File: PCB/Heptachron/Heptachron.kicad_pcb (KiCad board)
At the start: 2 copper layers, 50 x 42 mm, 13 parts, among them J1 Conn_01x06_Pin, J2 Conn_01x06_Pin

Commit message: Test PCB finished!
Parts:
- removed J2: Conn_01x06_Pin, Connector_Wire:SolderWire-0.1sqmm_1x06_P3.6mm_D0.4mm_OD1mm_Relief
- added C1: 100n, Capacitor_SMD:C_0603_1608Metric, F.Cu at (168.6, 119.5)
- added C2: 4.7u, Capacitor_SMD:C_0805_2012Metric, F.Cu at (125.5, 84.8)
- added C3: 4.7u, Capacitor_SMD:C_0805_2012Metric, F.Cu at (135.7, 81.5)
- added C4: 100n, Capacitor_SMD:C_0603_1608Metric, F.Cu at (147.5, 115.5)
- added C5: 4.7u, Capacitor_SMD:C_0805_2012Metric, F.Cu at (130.8, 88.5)
- added C6: 100n, Capacitor_SMD:C_0603_1608Metric, F.Cu at (127.1, 109.3)
- added C7: 100n, Capacitor_SMD:C_0603_1608Metric, F.Cu at (156.8, 90.7)
- added D1: PGD, LED_SMD:LED_0603_1608Metric, F.Cu at (146.1, 79.5)
- added D2: CHG, LED_SMD:LED_0603_1608Metric, F.Cu at (142.2, 79.5)
- added D3: BAT, LED_SMD:LED_0603_1608Metric, F.Cu at (154.0, 79.5)
- added D4: VCC, LED_SMD:LED_0603_1608Metric, F.Cu at (150.1, 79.5)
- added Q1: Q_Photo, LED_SMD:LED_0603_1608Metric, F.Cu at (133.2, 109.2)
- added R1: 10K, Resistor_SMD:R_0603_1608Metric, F.Cu at (165.7, 122.7)
- added R10: 1K, Resistor_SMD:R_0603_1608Metric, F.Cu at (142.2, 77.6)
- added R11: 1K, Resistor_SMD:R_0603_1608Metric, F.Cu at (154.0, 77.6)
- added R12: 1K, Resistor_SMD:R_0603_1608Metric, F.Cu at (150.1, 77.6)
- added R13: 2K, Resistor_SMD:R_0603_1608Metric, F.Cu at (153.9, 126.3)
- added R14: 2K, Resistor_SMD:R_0603_1608Metric, F.Cu at (153.9, 123.1)
- added R15: 10K, Resistor_SMD:R_0603_1608Metric, F.Cu at (159.7, 93.6)
- added R16: 10K, Resistor_SMD:R_0603_1608Metric, F.Cu at (130.1, 109.2)
- added R2: 10K, Resistor_SMD:R_0603_1608Metric, F.Cu at (165.7, 116.5)
- added R3: 10K, Resistor_SMD:R_0603_1608Metric, F.Cu at (125.5, 81.2)
- added R4: 10K, Resistor_SMD:R_0603_1608Metric, F.Cu at (125.5, 82.9)
- added R5: 3.3K, Resistor_SMD:R_0603_1608Metric, F.Cu at (128.8, 88.3)
- added R6: 4.7K, Resistor_SMD:R_0603_1608Metric, F.Cu at (135.7, 85.2)
- added R7: DNP, Resistor_SMD:R_0603_1608Metric, F.Cu at (132.7, 88.4)
- added R8: 10K, Resistor_SMD:R_0603_1608Metric, F.Cu at (135.7, 83.5)
- added R9: 1K, Resistor_SMD:R_0603_1608Metric, F.Cu at (146.1, 77.6)
- added SW1: SW_Push, Button_Switch_SMD:SW_Push_1P1T_NO_6x6mm_H9.5mm, F.Cu at (136.2, 126.5)
- added SW2: SW_Push, Button_Switch_SMD:SW_Push_1P1T_NO_6x6mm_H9.5mm, F.Cu at (125.5, 126.5)
- added SW4: SW_SP3T, Heptachron-Lib:sp3t_jumpers, F.Cu at (121.7, 90.3)
- added U6: BQ24230RGT, Package_DFN_QFN:VQFN-16-1EP_3x3mm_P0.5mm_EP1.68x1.68mm_ThermalVias, F.Cu at (130.8, 83.3)
- added U7: IS31FL3729, Package_QFP:TQFP-32_7x7mm_P0.8mm, F.Cu at (163.5, 86.9)
- added U8: ATtiny424-SS, Package_SO:SOIC-14_3.9x8.7mm_P1.27mm, F.Cu at (147.5, 121.5)
- added X1: RV-3028-C7, Heptachron-Lib:RV-3028-C7, F.Cu at (165.7, 119.5)
- J1: value Conn_01x06_Pin -> Conn_02x03_Counter_Clockwise; footprint Connector_Wire:SolderWire-0.1sqmm_1x06_P3.6mm_D0.4mm_OD1mm_Relief -> Connector_PinHeader_2.54mm:PinHeader_2x03_P2.54mm_Vertical
- moved D38 8.00 mm to (152.0, 108.0), turned to -90 degrees
- moved D42 8.00 mm to (144.0, 108.0), turned to -90 degrees
- moved J1 7.10 mm to (131.3, 120.3), turned to 180 degrees
- moved D39 4.00 mm to (150.0, 108.0), turned to -90 degrees
- moved D41 4.00 mm to (146.0, 108.0), turned to -90 degrees
- turned D40 to -90 degrees
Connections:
- D36 pad 1: /CS5 -> /CS7
- D36 pad 2: /SW6 -> /SW5
- D37 pad 1: /CS5 -> /CS6
- D37 pad 2: /SW7 -> /SW5
- D38 pad 1: /CS5 -> /CS1
- D38 pad 2: /SW1 -> /SW5
- D39 pad 1: /CS5 -> /CS2
- D39 pad 2: /SW2 -> /SW5
- D40 pad 1: /CS5 -> /CS3
- D40 pad 2: /SW3 -> /SW5
- D41 pad 1: /CS5 -> /CS4
- D41 pad 2: /SW4 -> /SW5
- J1 pad 1: /SW1 -> /UPDI
- J1 pad 2: /SW2 -> +BATT
- J1 pad 3: /SW3 -> /TX
- J1 pad 4: /SW4 -> +5V
- J1 pad 5: /SW5 -> /RX
- J1 pad 6: /SW6 -> GND
- U1 pad 1: /SW1 -> /SW4
- U1 pad 10: /CS1 -> /CS3
- U1 pad 11: /CS1 -> /CS4
- U1 pad 12: /CS1 -> /CS5
- U1 pad 13: /CS1 -> /CS6
- U1 pad 14: /CS1 -> /CS7
- U1 pad 2: /SW2 -> /SW4
- U1 pad 3: /SW3 -> /SW4
- U1 pad 5: /SW5 -> /SW4
- U1 pad 6: /SW6 -> /SW4
- U1 pad 7: /SW7 -> /SW4
- U1 pad 9: /CS1 -> /CS2
- U2 pad 1: /SW1 -> /SW3
- U2 pad 10: /CS2 -> /CS3
- U2 pad 11: /CS2 -> /CS4
- U2 pad 12: /CS2 -> /CS5
- U2 pad 13: /CS2 -> /CS6
- U2 pad 14: /CS2 -> /CS7
- U2 pad 2: /SW2 -> /SW3
- U2 pad 4: /SW4 -> /SW3
- U2 pad 5: /SW5 -> /SW3
- U2 pad 6: /SW6 -> /SW3
- U2 pad 7: /SW7 -> /SW3
- U2 pad 8: /CS2 -> /CS1
- U3 pad 1: /SW1 -> /SW2
- U3 pad 11: /CS3 -> /CS4
- U3 pad 12: /CS3 -> /CS5
- U3 pad 13: /CS3 -> /CS6
- U3 pad 14: /CS3 -> /CS7
- U3 pad 3: /SW3 -> /SW2
- U3 pad 4: /SW4 -> /SW2
- U3 pad 5: /SW5 -> /SW2
- U3 pad 6: /SW6 -> /SW2
- U3 pad 7: /SW7 -> /SW2
- U3 pad 8: /CS3 -> /CS1
- U3 pad 9: /CS3 -> /CS2
- U4 pad 10: /CS4 -> /CS3
- U4 pad 12: /CS4 -> /CS5
- U4 pad 13: /CS4 -> /CS6
- U4 pad 14: /CS4 -> /CS7
- U4 pad 2: /SW2 -> /SW1
- U4 pad 3: /SW3 -> /SW1
- U4 pad 4: /SW4 -> /SW1
- U4 pad 5: /SW5 -> /SW1
- U4 pad 6: /SW6 -> /SW1
- U4 pad 7: /SW7 -> /SW1
- U4 pad 8: /CS4 -> /CS1
- U4 pad 9: /CS4 -> /CS2
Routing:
- net VCC: track 0.00 -> 172.7 mm, vias 0 -> 5
- net +BATT: track 0.00 -> 89.3 mm, vias 0 -> 3
- net /PGOOD: track 0.00 -> 83.7 mm
- net GND: track 0.00 -> 76.7 mm, vias 0 -> 17
- net /SW6: track 74.9 -> 0.00 mm, vias 4 -> 0
- net /SDA: track 0.00 -> 72.7 mm, vias 0 -> 4
- net /SCL: track 0.00 -> 69.2 mm, vias 0 -> 4
- net /SW2: track 102.4 -> 37.1 mm, vias 2 -> 0
- net /LED_EN: track 0.00 -> 65.0 mm, vias 0 -> 4
- net /SW7: track 60.1 -> 0.00 mm, vias 8 -> 0
- net /CS7: track 0.00 -> 58.5 mm, vias 0 -> 6
- net /CS6: track 0.00 -> 58.2 mm, vias 0 -> 5
- net /SW1: track 96.8 -> 43.2 mm, vias 9 -> 0
- net +5V: track 0.00 -> 44.9 mm, vias 0 -> 1
- net /SW3: track 77.9 -> 43.5 mm, vias 7 -> 0
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- added copper zone on B.Cu, net GND
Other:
- board size 50 x 42 mm -> 55.2 x 55.2 mm
- board text added: "+5V"
- board text added: "+BAT"
- board text added: "+BMS"
- board text added: "GND"
- board text added: "HEPTACHRON alpha1 Adam Anderson Gustav Abrahamsson 2024"
- board text added: "JLCJLCJLCJLC"
- board text added: "RX"
- board text added: "TX"
- board text added: "UPDI"
- board text removed: "SW1 SW2 SW3 SW4 SW5 SW6"
- board text removed: "SW7 CS1 CS2 CS3 CS4 CS5"

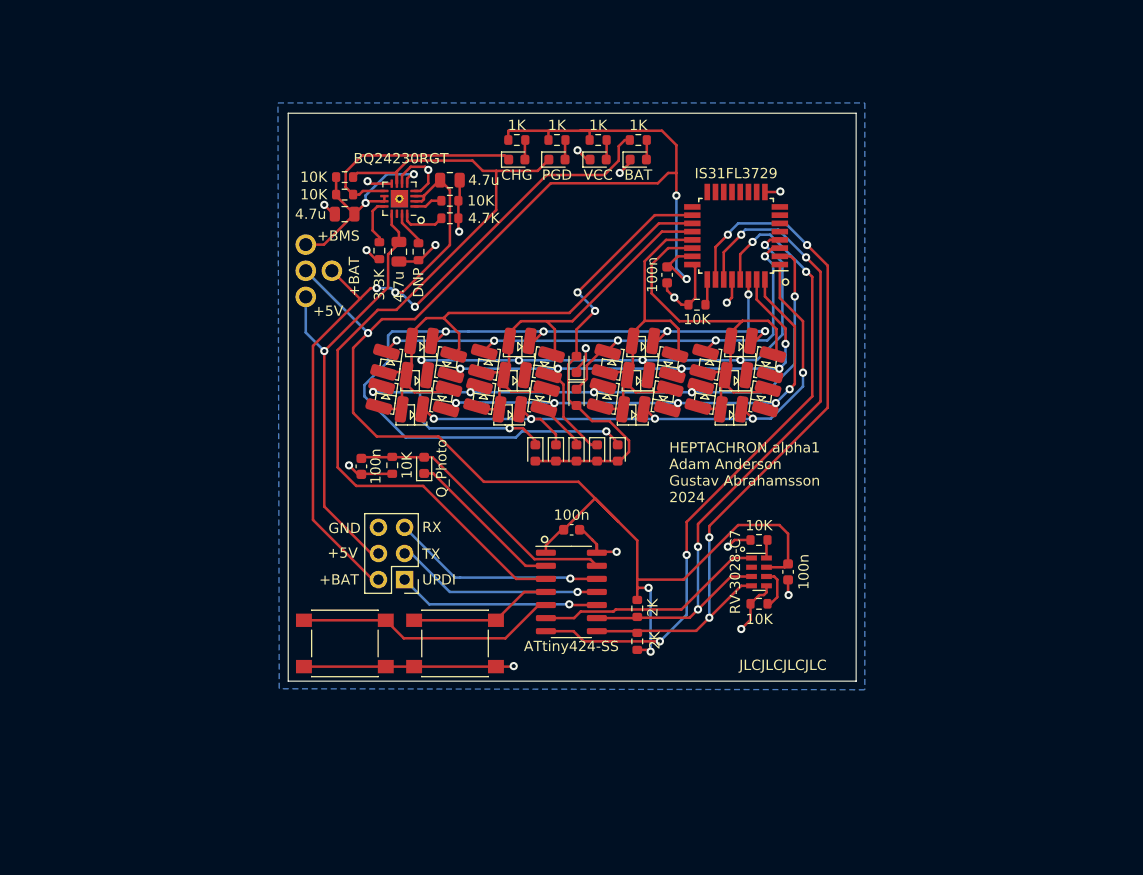
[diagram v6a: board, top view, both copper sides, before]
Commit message: Add testing PCB [Ordered]
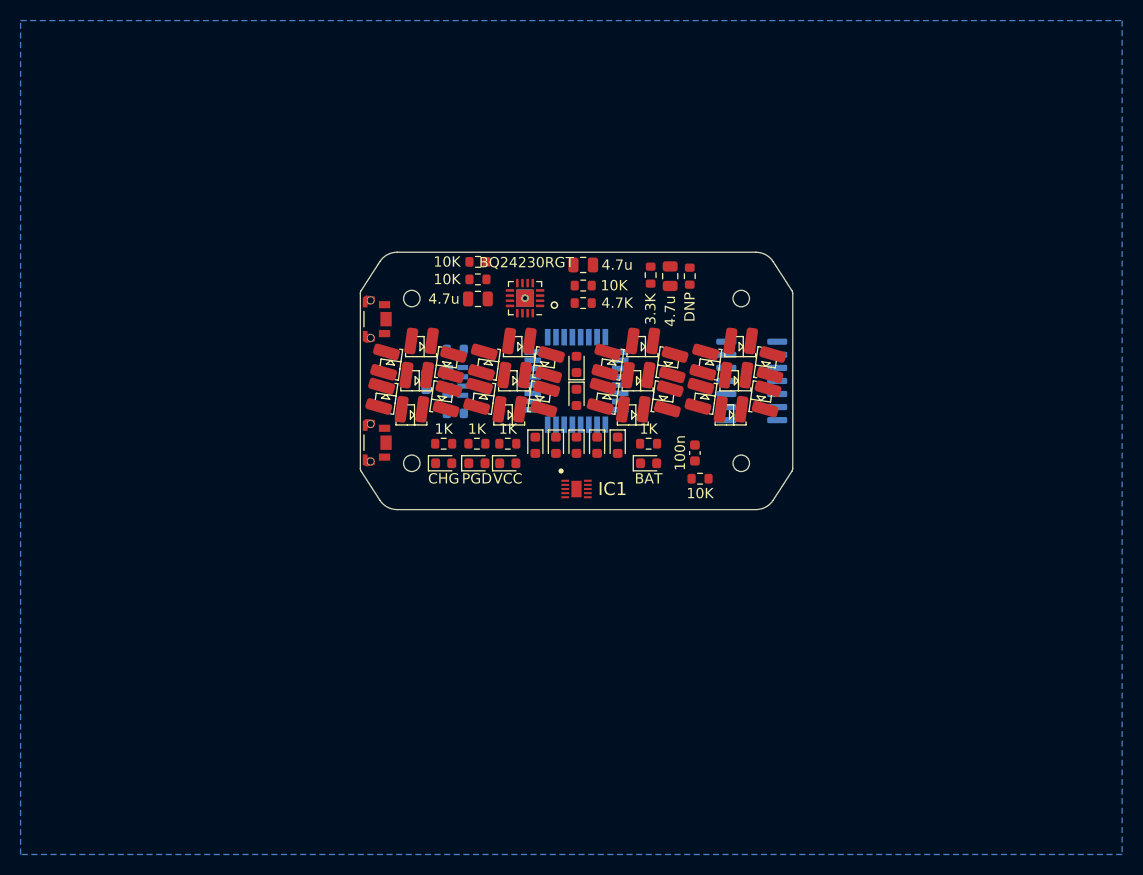
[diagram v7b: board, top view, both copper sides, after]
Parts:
- removed C4, C6: 100n, Capacitor_SMD:C_0603_1608Metric
- removed J1: Conn_02x03_Counter_Clockwise, Connector_PinHeader_2.54mm:PinHeader_2x03_P2.54mm_Vertical
- removed Q1: Q_Photo, LED_SMD:LED_0603_1608Metric
- removed R13, R14: 2K, Resistor_SMD:R_0603_1608Metric
- removed R16: 10K, Resistor_SMD:R_0603_1608Metric
- removed SW4: SW_SP3T, Heptachron-Lib:sp3t_jumpers
- added IC1: BQ25185DLHR, Heptachron-Lib:SON40P220X200X80-11N, F.Cu at (148.0, 111.5)
- C1, R1, R2, U7, U8, X1: moved to B.Cu
- SW1, SW2: footprint Button_Switch_SMD:SW_Push_1P1T_NO_6x6mm_H9.5mm -> Heptachron-Lib:SW_TL6340AF160Q
- moved C1 39.7 mm to (133.4, 101.0)
- moved R1 34.8 mm to (136.2, 104.2), turned to 180 degrees
- moved R2 34.8 mm to (136.2, 98.0), turned to 180 degrees
- moved X1 34.8 mm to (136.2, 101.0)
- moved SW1 32.5 mm to (128.0, 95.0), turned to 90 degrees
- moved D4 30.8 mm to (141.3, 109.0)
- moved R12 30.8 mm to (141.3, 107.1)
- moved D1 30.5 mm to (138.3, 109.0)
- moved R9 30.5 mm to (138.3, 107.1)
- moved D2 30.3 mm to (135.1, 109.0)
- moved R10 30.3 mm to (135.1, 107.1)
- moved D3 29.5 mm to (155.0, 109.0)
- moved R11 29.5 mm to (155.0, 107.1)
- moved U8 27.0 mm to (165.0, 101.0), turned to 180 degrees
- moved C5 26.5 mm to (157.1, 90.8)
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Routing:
- net VCC: track 172.7 -> 0.00 mm, vias 5 -> 0
- net +BATT: track 89.3 -> 0.00 mm, vias 3 -> 0
- net /CS1: track 84.7 -> 0.00 mm, vias 6 -> 0
- net /PGOOD: track 83.7 -> 0.00 mm
- net GND: track 76.7 -> 0.00 mm, vias 17 -> 0
- net /CS5: track 73.0 -> 0.00 mm, vias 6 -> 0
- net /SDA: track 72.7 -> 0.00 mm, vias 4 -> 0
- net /SCL: track 69.2 -> 0.00 mm, vias 4 -> 0
- net /LED_EN: track 65.0 -> 0.00 mm, vias 4 -> 0
- net /CS4: track 63.8 -> 0.00 mm, vias 5 -> 0
- net /CS7: track 58.5 -> 0.00 mm, vias 6 -> 0
- net /CS6: track 58.2 -> 0.00 mm, vias 5 -> 0
- net /CS2: track 55.2 -> 0.00 mm, vias 5 -> 0
- net /CS3: track 54.8 -> 0.00 mm, vias 5 -> 0
- net /SW4: track 54.0 -> 0.00 mm
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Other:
- board size 55.2 x 55.2 mm -> 42 x 25 mm
- board text added: "TEST BOARD, NOT FUNCTIONAL"
- board text removed: "+5V"
- board text removed: "+BAT"
- board text removed: "+BMS"
- board text removed: "GND"
- board text removed: "HEPTACHRON alpha1 Adam Anderson Gustav Abrahamsson 2024"
- board text removed: "RX"
- board text removed: "TX"
- board text removed: "UPDI"
- board text removed: "__ ____________ _________ ________ ______ ____ _ __ / / / / ____/ __ \/_ __/ | / ____/ / / / __ \/ __ \/ | / / / /_/ / __/ / /_/ / / / / /| |/ / / /_/ / /_/ / / / / |/ / / __ / /___/ ____/ / / / ___ / /___/ __ / _, _/ /_/ / /| / /_/ /_/_____/_/ /_/ /_/ |_\____/_/ /_/_/ |_|\____/_/ |_/"

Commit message: Continue PCB
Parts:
- added C4: 100n, Capacitor_SMD:C_0603_1608Metric, F.Cu at (109.9, 95.1)
- added C6: 100n, Capacitor_SMD:C_0603_1608Metric, F.Cu at (109.9, 97.6)
- added J2: Conn_01x01_Pin, Connector_Wire:SolderWirePad_1x01_SMD_1x2mm, F.Cu at (120.5, 82.0)
- added Q1: Q_Photo_NPN, LED_SMD:LED_0603_1608Metric, F.Cu at (114.0, 104.3)
- added R13: 2K, Resistor_SMD:R_0603_1608Metric, F.Cu at (109.9, 100.1)
- added R14: 2K, Resistor_SMD:R_0603_1608Metric, F.Cu at (109.9, 102.6)
- added R16: 10K, Resistor_SMD:R_0603_1608Metric, F.Cu at (109.9, 105.1)
- added SW4: SW_SP3T, Heptachron-Lib:sp3t_jumpers, F.Cu at (116.0, 101.5)
